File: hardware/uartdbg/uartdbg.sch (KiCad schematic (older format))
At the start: 2 parts

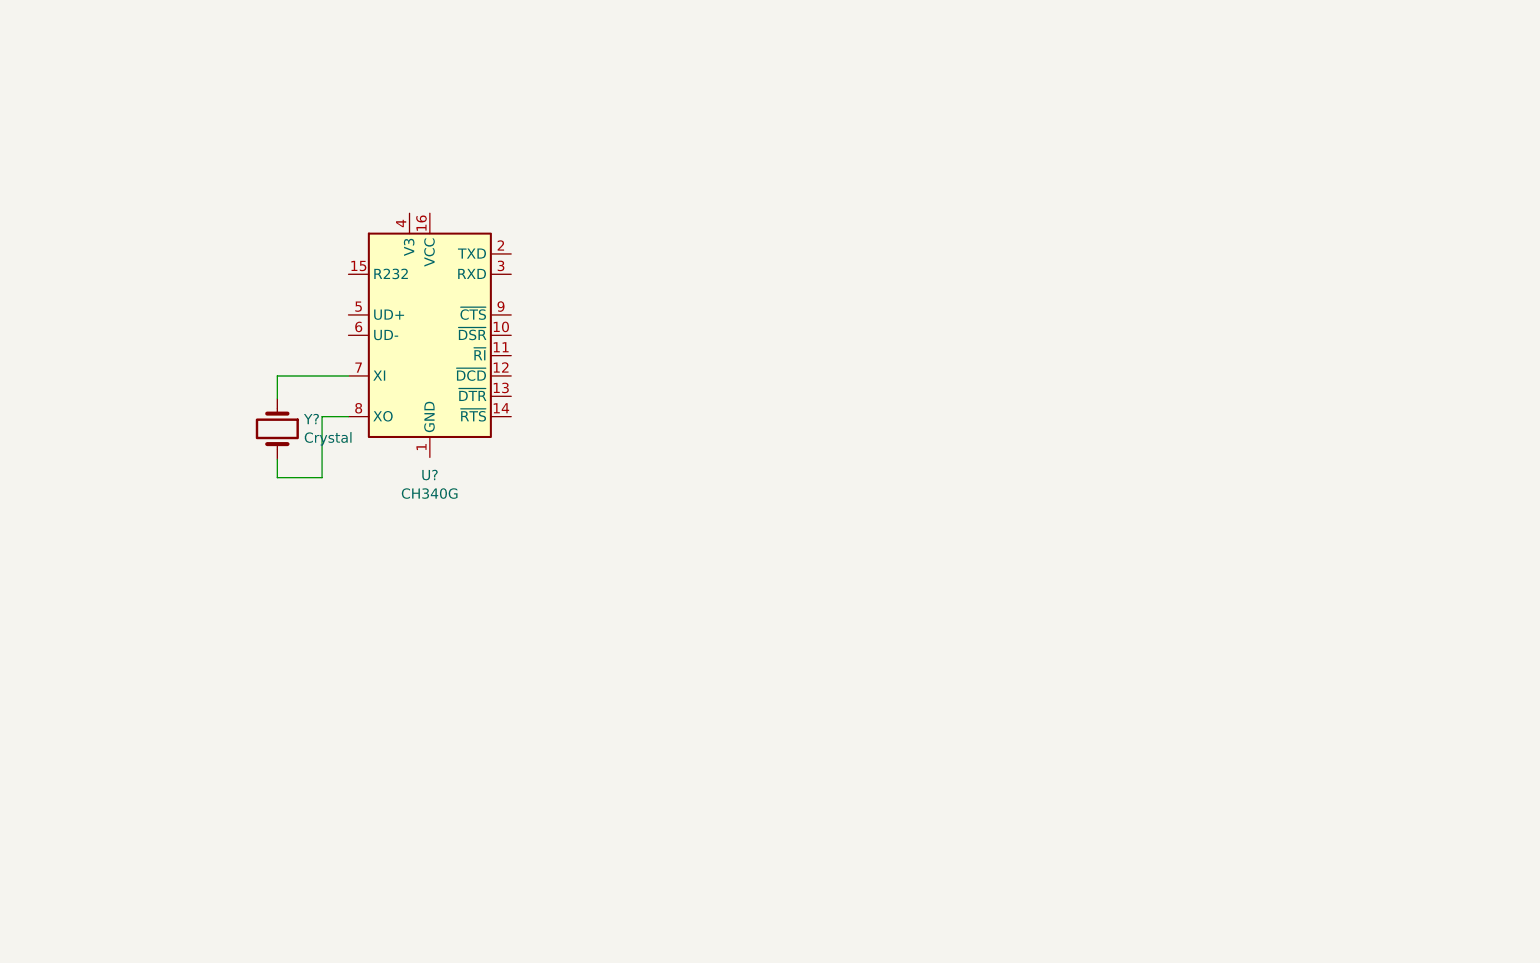
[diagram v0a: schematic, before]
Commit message: [ADD][CHG][NT] 更新原理图和 3D 封装库等内容
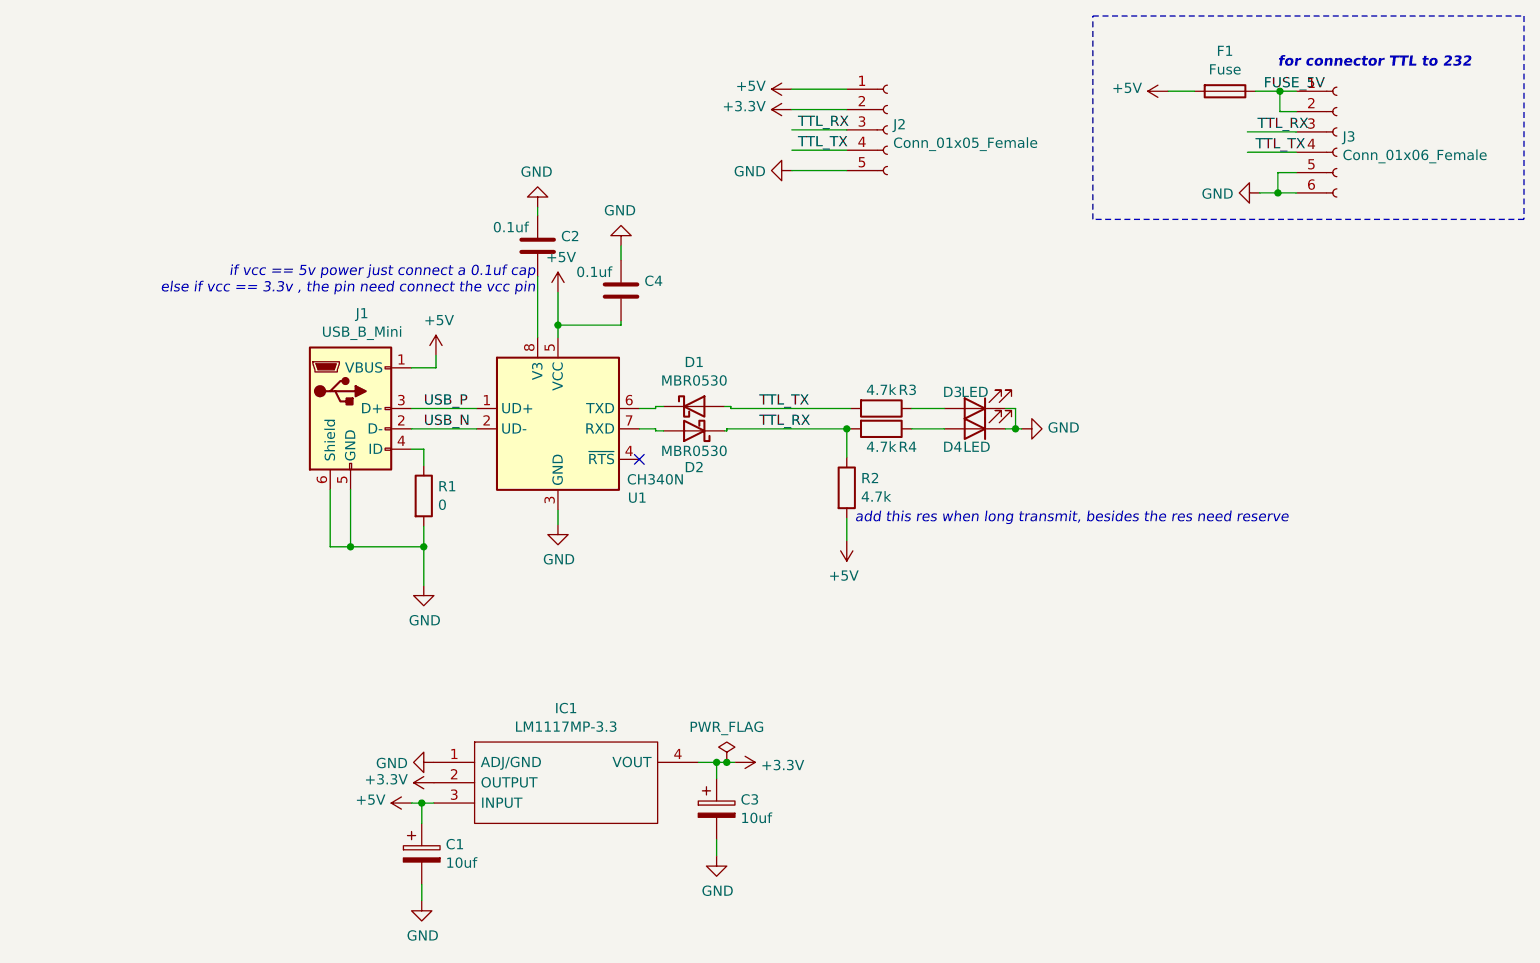
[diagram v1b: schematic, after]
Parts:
- removed U?: CH340G, Package_SO:SOIC-16_3.9x9.9mm_P1.27mm, symbol Interface_USB:CH340G
- removed Y?: Crystal, symbol Device:Crystal
- added C1, C3: 10uf, Red_Pro:CP_EIA-7343-31_Kemet-D_Pad2.25x2.55mm_HandSolder, symbol Device:CP
- added C2, C4: 0.1uf, Red_Pro:C_0603_1608Metric_Pad1.08x0.95mm_HandSolder, symbol Device:C
- added D1, D2: MBR0530, Red_Pro:D_SOD-123, symbol Diode:MBR0530
- added D3, D4: LED, LED_SMD:LED_0603_1608Metric_Pad1.05x0.95mm_HandSolder, symbol Device:LED
- added F1: Fuse, Red_Pro:Fuse_1206_3216Metric_Pad1.42x1.75mm_HandSolder, symbol Device:Fuse
- added IC1: LM1117MP-3.3, Red_Pro:SOT230P700X180-4N, symbol Red_Pro:LM1117MP-3.3
- added J1: USB_B_Mini, Red_Pro:USB_Mini-B_Lumberg_2486_01_Horizontal, symbol Connector:USB_B_Mini
- added J2: Conn_01x05_Female, Red_Pro:PinHeader_1x05_P2.54mm_Vertical, symbol Connector:Conn_01x05_Female
- added J3: Conn_01x06_Female, Red_Pro:TE_84952-6_1x06-1MP_P1.0mm_Horizontal, symbol Connector:Conn_01x06_Female
- added R1: 0, Red_Pro:R_0603_1608Metric_Pad0.98x0.95mm_HandSolder, symbol Device:R
- added R2, R3, R4: 4.7k, Red_Pro:R_0603_1608Metric_Pad0.98x0.95mm_HandSolder, symbol Device:R
- added U1: CH340N, Red_Pro:SOIC-8-CH340N, symbol Red_Pro:CH340N
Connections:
- net labels added: +3.3V, +5V, FUSE_5V, GND, TTL_RX, TTL_TX, USB_N, USB_P
- wire segments 6 -> 66
- no-connect marks 0 -> 1
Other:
- note added: "add this res when long transmit, besides the res need reserve"
- note added: "for connector TTL to 232"
- note added: "if vcc == 5v power just connect a 0.1uf cap\nelse if vcc == 3.3v , the pin need connect the vcc pin"

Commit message: [CHG][ADD][NT] 更新原理图和 PCB,添加额外的保护以及 logo,添加 geber 文件包
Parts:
- added C5: 4.7nf, Red_Pro:C_0603_1608Metric_Pad1.08x0.95mm_HandSolder, symbol Device:C
- added LOGO1: Logo_Open_Hardware_Small, Symbol:OSHW-Logo2_7.3x6mm_Copper, symbol Graphic:Logo_Open_Hardware_Small
- added R5: 1M, Red_Pro:R_0603_1608Metric_Pad0.98x0.95mm_HandSolder, symbol Device:R
- D3, D4: footprint LED_SMD:LED_0603_1608Metric_Pad1.05x0.95mm_HandSolder -> Red_Pro:LED_0603_1608Metric_Pad1.05x0.95mm_HandSolder
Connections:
- wire segments 66 -> 74
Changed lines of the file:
@@
 F 3 "~" H 3110 3510 50  0001 C CNN
 	1    3110 3510
-	1    0    0    -1
+	1    0    0    1
 $EndComp
 $Comp
 L power:GND #PWR03
 U 1 1 60BE509E
-P 3110 3950
-F 0 "#PWR03" H 3110 3700 50  0001 C CNN
-F 1 "GND" H 3115 3777 50  0000 C CNN
-F 2 "" H 3110 3950 50  0001 C CNN
-F 3 "" H 3110 3950 50  0001 C CNN
-	1    3110 3950
+P 3110 4160
+F 0 "#PWR03" H 3110 3910 50  0001 C CNN
+F 1 "GND" H 3115 3987 50  0000 C CNN
+F 2 "" H 3110 4160 50  0001 C CNN
+F 3 "" H 3110 4160 50  0001 C CNN
+	1    3110 4160
 	1    0    0    -1
 $EndComp
@@
 Connection ~ 3110 3760
 Wire Wire Line
-	3110 3760 3110 3950
-Wire Wire Line
-	2650 3480 2650 3760
-Wire Wire Line
-	2650 3760 2750 3760
-Connection ~ 2750 3760
+	3110 3760 3110 4020
 $Comp
 L power:+5V #PWR06
@@
 F 0 "D3" H 5930 3000 50  0000 C CNN
 F 1 "LED" H 5820 3000 50  0000 C CNN
-F 2 "LED_SMD:LED_0603_1608Metric_Pad1.05x0.95mm_HandSolder" H 5820 3080 50  0001 C CNN
+F 2 "Red_Pro:LED_0603_1608Metric_Pad1.05x0.95mm_HandSolder" H 5820 3080 50  0001 C CNN
 F 3 "~" H 5820 3080 50  0001 C CNN
 	1    5820 3080
@@
 F 0 "D4" H 5930 3270 50  0000 C CNN
 F 1 "LED" H 5810 3270 50  0000 C CNN
-F 2 "LED_SMD:LED_0603_1608Metric_Pad1.05x0.95mm_HandSolder" H 5820 3180 50  0001 C CNN
+F 2 "Red_Pro:LED_0603_1608Metric_Pad1.05x0.95mm_HandSolder" H 5820 3180 50  0001 C CNN
 F 3 "~" H 5820 3180 50  0001 C CNN
 	1    5820 3180
@@
 Text Label 7240 1520 0    50   ~ 0
 FUSE_5V
+$Comp
+L Device:R R5
+U 1 1 60C29019
+P 2480 3750
+F 0 "R5" H 2550 3796 50  0000 L CNN
+F 1 "1M" H 2550 3705 50  0000 L CNN
+F 2 "Red_Pro:R_0603_1608Metric_Pad0.98x0.95mm_HandSolder" V 2410 3750 50  0001 C CNN
+F 3 "~" H 2480 3750 50  0001 C CNN
+	1    2480 3750
+	1    0    0    1
+$EndComp
+$Comp
+L Device:C C5
+U 1 1 60C29781
+P 2240 3740
+F 0 "C5" H 2270 3830 50  0000 L CNN
+F 1 "4.7nf" H 2020 3830 50  0000 L CNN
+F 2 "Red_Pro:C_0603_1608Metric_Pad1.08x0.95mm_HandSolder" H 2278 3590 50  0001 C CNN
+F 3 "~" H 2240 3740 50  0001 C CNN
+	1    2240 3740
+	1    0    0    -1
+$EndComp
+Wire Wire Line
+	2480 3900 2480 4020
+Wire Wire Line
+	2480 4020 3110 4020
+Connection ~ 3110 4020
+Wire Wire Line
+	3110 4020 3110 4160
+Wire Wire Line
+	2240 3890 2240 4020
+Wire Wire Line
+	2240 4020 2480 4020
+Connection ~ 2480 4020
+Wire Wire Line
+	2650 3480 2650 3500
+Wire Wire Line
+	2650 3500 2480 3500
+Wire Wire Line
+	2240 3500 2240 3590
+Wire Wire Line
+	2480 3600 2480 3500
+Connection ~ 2480 3500
+Wire Wire Line
+	2480 3500 2240 3500
+$Comp
+L Graphic:SYM_ESD_Large #SYM1
+U 1 1 60BF7AAF
+P 4290 3890
+F 0 "#SYM1" H 4290 4120 50  0001 C CNN
+F 1 "SYM_ESD_Large" H 4290 3640 50  0001 C CNN
+F 2 "Symbol:OSHW-Logo2_7.3x6mm_Copper" H 4285 3860 50  0001 C CNN
+F 3 "~" H 4285 3860 50  0001 C CNN
+	1    4290 3890
+	1    0    0    -1
+$EndComp
+$Comp
+L Graphic:Logo_Open_Hardware_Small LOGO1
+U 1 1 60C097C6
+P 7960 3040
+F 0 "LOGO1" H 7960 3315 50  0001 C CNN
+F 1 "Logo_Open_Hardware_Small" H 7960 2815 50  0001 C CNN
+F 2 "Symbol:OSHW-Logo2_7.3x6mm_Copper" H 7960 3040 50  0001 C CNN
+F 3 "~" H 7960 3040 50  0001 C CNN
+	1    7960 3040
+	1    0    0    -1
+$EndComp
 $EndSCHEMATC

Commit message: [CHG][NT] 更新原理图和 PCB 对 TX 和 RX LED 灯具状态指示管脚接线为上拉
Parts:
- R3, R4: value 4.7k -> 510
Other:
- moved on the sheet: D3, D4
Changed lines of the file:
@@
 P 5360 3080
 F 0 "R3" V 5270 3210 50  0000 C CNN
-F 1 "4.7k" V 5270 3080 50  0000 C CNN
+F 1 "510" V 5270 3080 50  0000 C CNN
 F 2 "Red_Pro:R_0603_1608Metric_Pad0.98x0.95mm_HandSolder" V 5290 3080 50  0001 C CNN
 F 3 "~" H 5360 3080 50  0001 C CNN
@@
 U 1 1 60C134D9
 P 5820 3080
-F 0 "D3" H 5930 3000 50  0000 C CNN
-F 1 "LED" H 5820 3000 50  0000 C CNN
+F 0 "D3" H 5920 3130 50  0000 C CNN
+F 1 "LED" H 5810 3170 50  0000 C CNN
 F 2 "Red_Pro:LED_0603_1608Metric_Pad1.05x0.95mm_HandSolder" H 5820 3080 50  0001 C CNN
 F 3 "~" H 5820 3080 50  0001 C CNN
 	1    5820 3080
-	-1   0    0    1
+	1    0    0    -1
 $EndComp
 Wire Wire Line
@@
 P 5360 3180
 F 0 "R4" V 5450 3310 50  0000 C CNN
-F 1 "4.7k" V 5450 3180 50  0000 C CNN
+F 1 "510" V 5450 3180 50  0000 C CNN
 F 2 "Red_Pro:R_0603_1608Metric_Pad0.98x0.95mm_HandSolder" V 5290 3180 50  0001 C CNN
 F 3 "~" H 5360 3180 50  0001 C CNN
@@
 	0    1    1    0
 $EndComp
-$Comp
-L Device:LED D4
-U 1 1 60C192DA
-P 5820 3180
-F 0 "D4" H 5930 3270 50  0000 C CNN
-F 1 "LED" H 5810 3270 50  0000 C CNN
-F 2 "Red_Pro:LED_0603_1608Metric_Pad1.05x0.95mm_HandSolder" H 5820 3180 50  0001 C CNN
-F 3 "~" H 5820 3180 50  0001 C CNN
-	1    5820 3180
-	-1   0    0    1
-$EndComp
 Wire Wire Line
 	5510 3180 5670 3180
@@
 	5210 3180 5190 3180
 Connection ~ 5190 3180
-$Comp
-L power:GND #PWR014
-U 1 1 60C1EDE7
-P 6050 3180
-F 0 "#PWR014" H 6050 2930 50  0001 C CNN
-F 1 "GND" V 6055 3052 50  0000 R CNN
-F 2 "" H 6050 3180 50  0001 C CNN
-F 3 "" H 6050 3180 50  0001 C CNN
-	1    6050 3180
-	0    -1   -1   0
-$EndComp
 Wire Wire Line
 	6050 3180 6020 3180
@@
 	1    0    0    -1
 $EndComp
+$Comp
+L Device:LED D4
+U 1 1 60C192DA
+P 5820 3180
+F 0 "D4" H 5940 3140 50  0000 C CNN
+F 1 "LED" H 5810 3090 50  0000 C CNN
+F 2 "Red_Pro:LED_0603_1608Metric_Pad1.05x0.95mm_HandSolder" H 5820 3180 50  0001 C CNN
+F 3 "~" H 5820 3180 50  0001 C CNN
+	1    5820 3180
+	1    0    0    -1
+$EndComp
+$Comp
+L power:+5V #PWR?
+U 1 1 60C5D182
+P 6050 3180
+F 0 "#PWR?" H 6050 3030 50  0001 C CNN
+F 1 "+5V" H 6065 3353 50  0000 C CNN
+F 2 "" H 6050 3180 50  0001 C CNN
+F 3 "" H 6050 3180 50  0001 C CNN
+	1    6050 3180
+	0    1    1    0
+$EndComp
 $EndSCHEMATC
